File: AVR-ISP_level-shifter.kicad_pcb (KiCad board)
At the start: 2 copper layers, 44 x 20 mm, 27 parts, among them Q1 BSS138, Q2 BSS138, Q3 BSS138, Q4 BSS138, Q5 BSS138, Q6 BSS138, Q7 BSS138, Q8 BSS138, SW1 APEM 25439NH, U1 AMS1117-3.3

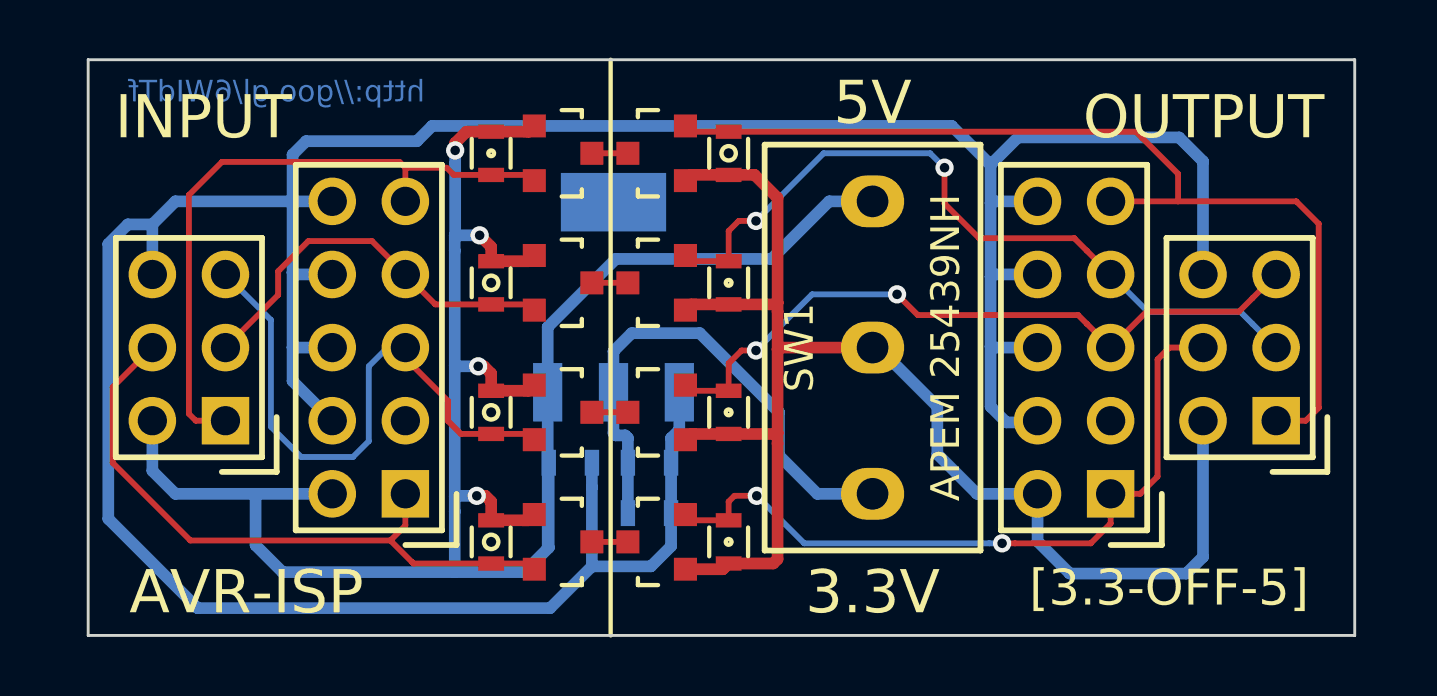
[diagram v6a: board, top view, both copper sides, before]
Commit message: Changed footprints for easier handsoldering + necessary tweaks.
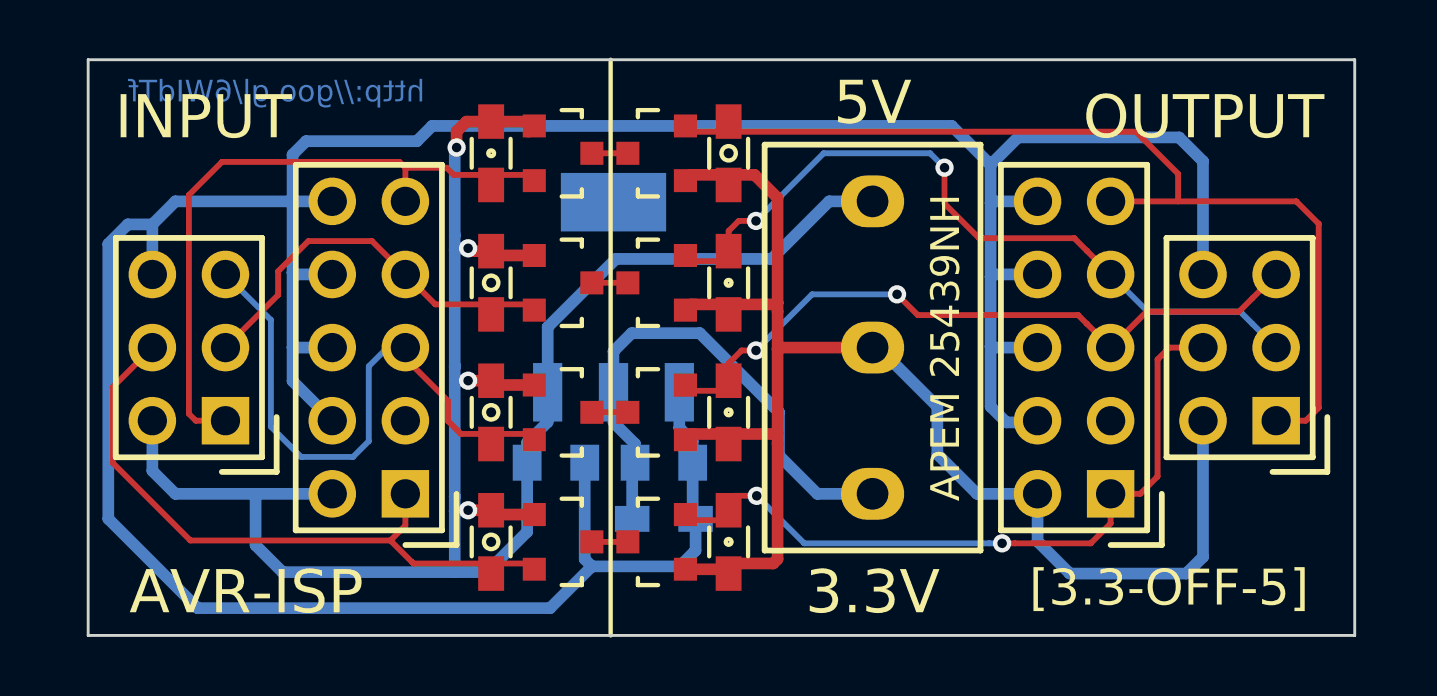
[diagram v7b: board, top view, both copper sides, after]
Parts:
- C1, C2: footprint Resistors_SMD:R_0603 -> Capacitors_SMD:C_0805
- DR.R2, DR.R3, DR.R5, DR.R7, R1, R4, R6, R8, R9: footprint Resistors_SMD:R_0603 -> Resistors_SMD:R_0603_HandSoldering
- moved R9 0.54 mm to (66.5, 55.2)
- moved C1 0.50 mm to (62.8, 53.2)
- moved C2 0.50 mm to (66.5, 53.2)
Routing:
- net /VCC_PRG: track 74.2 -> 68.3 mm
- net /GND: track 115.6 -> 116.8 mm
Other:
- board text added: "AVR-ISP level-shifter 0.12.b"
- board text removed: "AVR-ISP level-shifter 0.12.a"
